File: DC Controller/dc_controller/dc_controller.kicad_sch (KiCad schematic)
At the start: 34 parts, among them J1 Screw_Terminal_01x08, M1 Motor_DC, Q1 IRFB4110PBF NMOS, Q11 IRFB4110PBF NMOS, Q12 IRFB4110PBF NMOS, Q2 IRFB4110PBF NMOS, Q3 IRFB4110PBF NMOS, Q4 IRFB4110PBF NMOS, Q5 IRFB4110PBF NMOS, Q6 IRFB4110PBF NMOS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

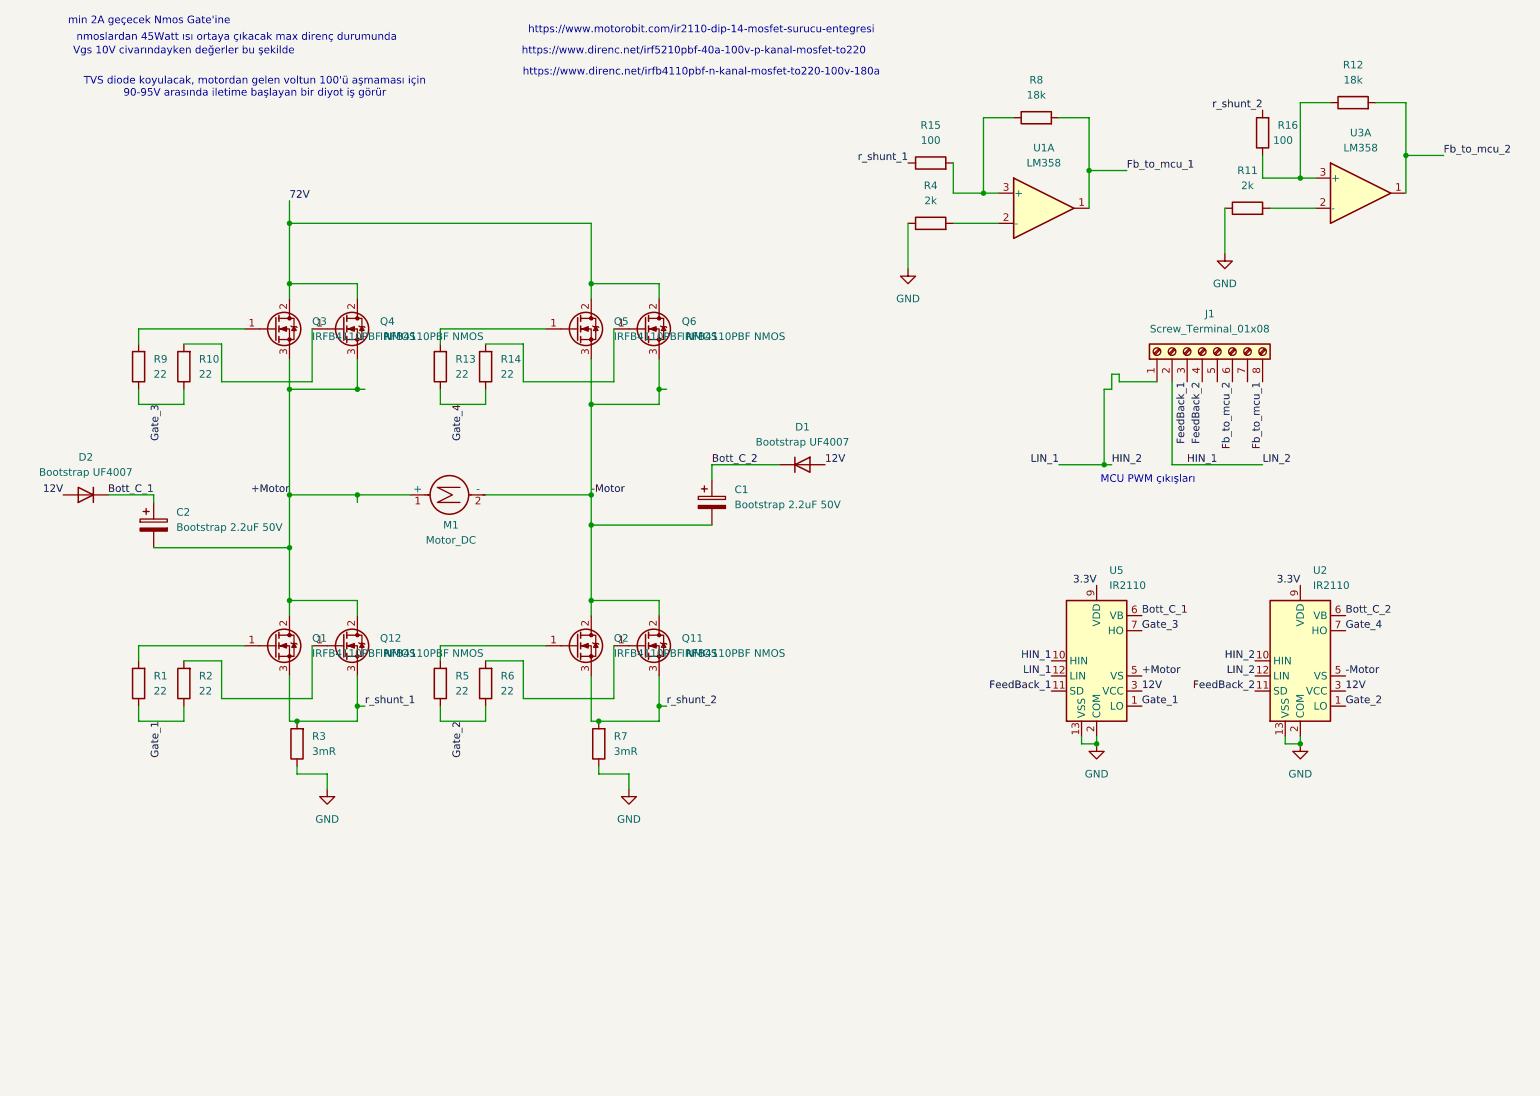
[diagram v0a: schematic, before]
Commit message: DC Sürücü
Mosfet sürücü bağlantıları güncellendi
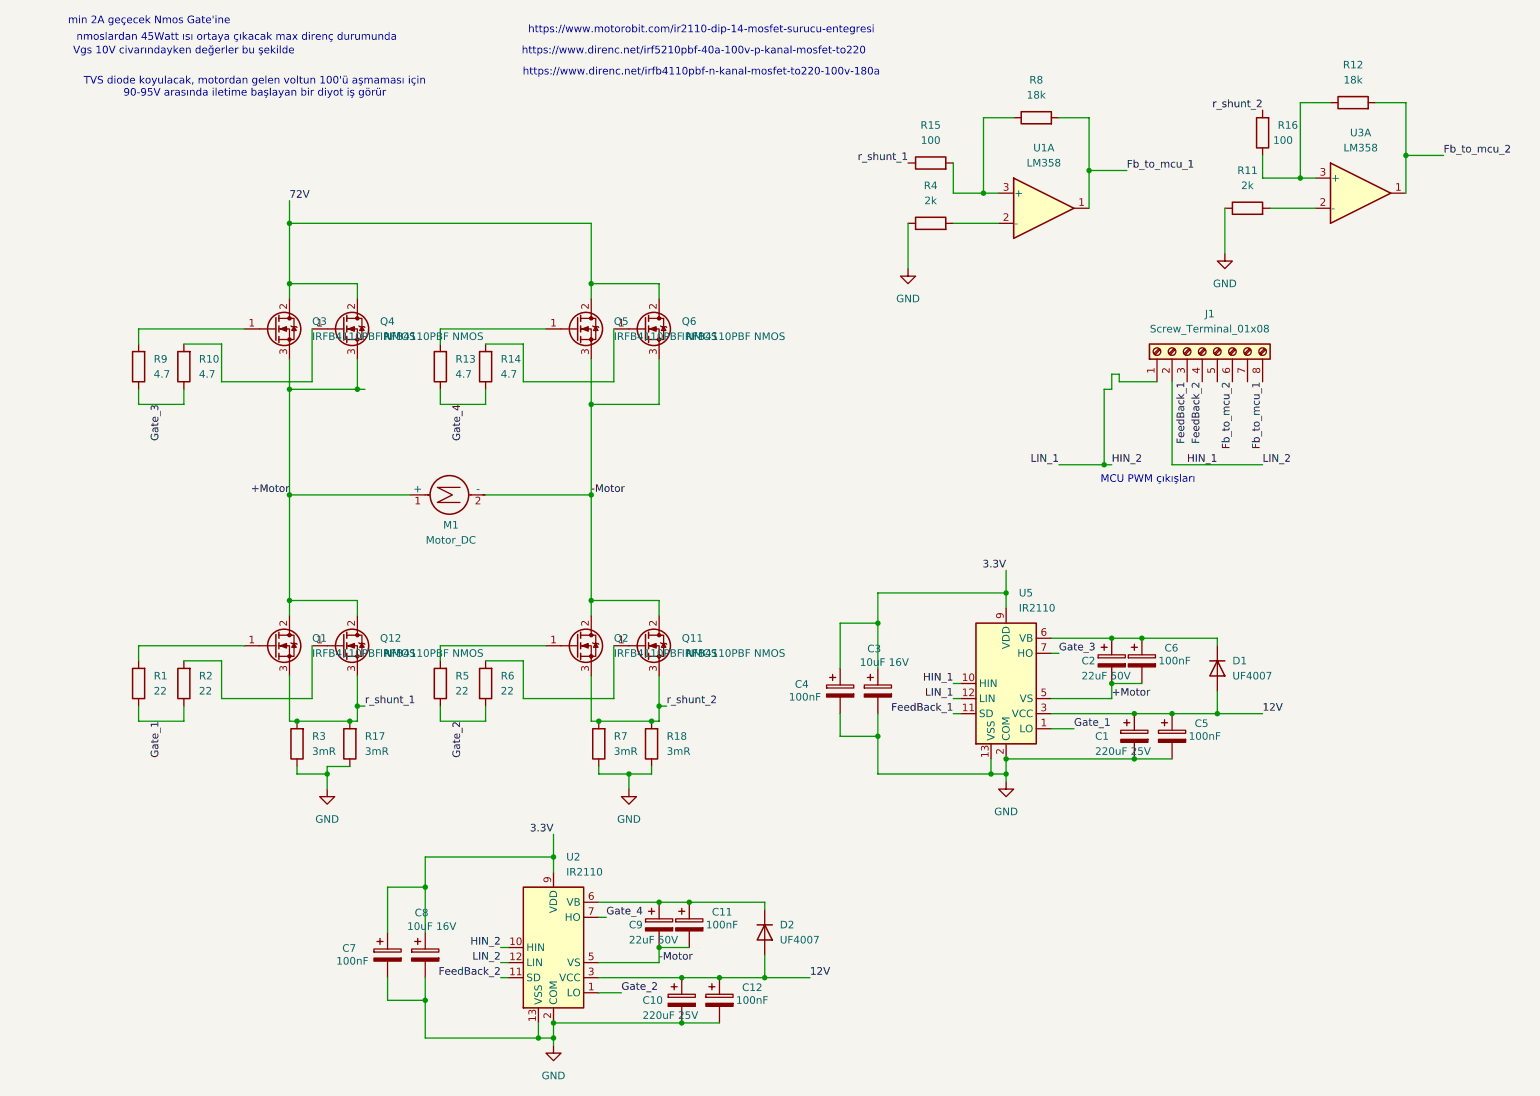
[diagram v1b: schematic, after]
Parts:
- added C10: 220uF 25V, symbol Device:C_Polarized
- added C11, C12, C4, C5, C6, C7: 100nF, symbol Device:C_Polarized
- added C3, C8: 10uF 16V, symbol Device:C_Polarized
- added C9: 22uF 50V, symbol Device:C_Polarized
- added R17, R18: 3mR, symbol Device:R
- C1: value Bootstrap 2.2uF 50V -> 220uF 25V
- C2: value Bootstrap 2.2uF 50V -> 22uF 50V
- D1, D2: value Bootstrap UF4007 -> UF4007
- R10, R13, R14, R9: value 22 -> 4.7
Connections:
- net +Motor: now also C6.2
- net -Motor: now also C11.2, C9.2; no longer C1.2
- net 12V: now also C1.1, C10.1, C12.1, C5.1
- net 3.3V: now also C3.1, C4.1, C7.1, C8.1
- net GND: now also C1.2, C10.2, C12.2, C3.2, C4.2, C5.2, C7.2, C8.2, R17.1, R18.1
- net r_shunt_1: now also R17.2
- net r_shunt_2: now also R18.2
- net Bott_C_1: no longer names the net of C2.1, U5.6 (VB)
- net Bott_C_1: now also D1.1 (K), C6.1; no longer D2.1 (K)
- removed net Bott_C_2: C1.1, D1.1 (K), U2.6 (VB)
- new net: C11.1, C9.1, D2.1 (K), U2.6 (VB)
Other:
- moved on the sheet: U5
